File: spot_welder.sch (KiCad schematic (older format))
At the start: 30 parts, among them J1 Conn_01x02_Female, J2 Conn_01x02_Female, J3 Supply, Q1 BSR20, Q2 BSR20, Q3 BSR20, SW1 Rotary_Encoder_Switch, U1 Stm8S103F6_module, U5 MOC3062M

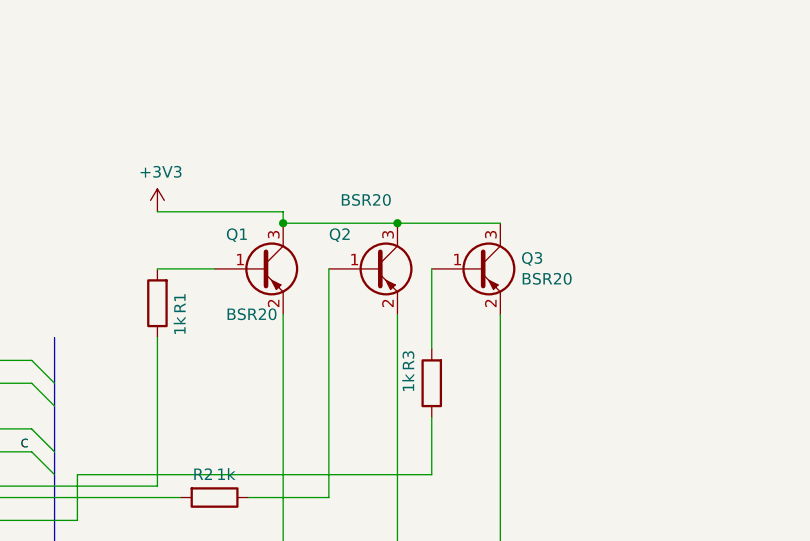
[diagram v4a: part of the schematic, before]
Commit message: clearances increased, vias enlarged
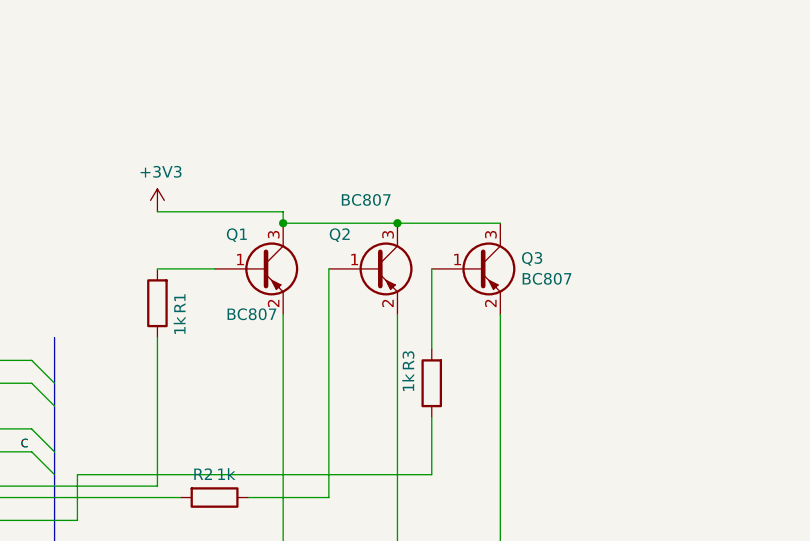
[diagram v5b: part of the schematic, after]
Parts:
- Q1, Q2, Q3: value BSR20 -> BC807
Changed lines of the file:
@@
 P 5000 2550
 F 0 "Q1" H 4850 2700 50  0000 L CNN
-F 1 "BSR20" H 4850 2350 50  0000 L CNN
+F 1 "BC807" H 4850 2350 50  0000 L CNN
 F 2 "Package_TO_SOT_SMD:SOT-23" H 5200 2650 50  0001 C CNN
 F 3 "~" H 5000 2550 50  0001 C CNN
@@
 P 5500 2550
 F 0 "Q2" H 5300 2700 50  0000 L CNN
-F 1 "BSR20" H 5350 2850 50  0000 L CNN
+F 1 "BC807" H 5350 2850 50  0000 L CNN
 F 2 "Package_TO_SOT_SMD:SOT-23" H 5700 2650 50  0001 C CNN
 F 3 "~" H 5500 2550 50  0001 C CNN
@@
 P 5950 2550
 F 0 "Q3" H 6141 2596 50  0000 L CNN
-F 1 "BSR20" H 6141 2505 50  0000 L CNN
+F 1 "BC807" H 6141 2505 50  0000 L CNN
 F 2 "Package_TO_SOT_SMD:SOT-23" H 6150 2650 50  0001 C CNN
 F 3 "~" H 5950 2550 50  0001 C CNN

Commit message: library name updated
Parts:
- D2: symbol marcin_schematic:SM410363 -> marcin_kicad_sch:SM410363
- U1: symbol marcin_schematic:Stm8S103F6_module -> marcin_kicad_sch:Stm8S103F6_module
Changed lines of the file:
@@
 EESchema Schematic File Version 4
-LIBS:spot_welder-cache
-EELAYER 26 0
+EELAYER 30 0
 EELAYER END
 $Descr A4 11693 8268
@@
 	2550 6250 2550 6300
 $Comp
-L marcin_schematic:Stm8S103F6_module U1
+L marcin_kicad_sch:Stm8S103F6_module U1
 U 1 1 5EED1B37
 P 2450 2950
@@
 	2200 2750 2200 2950
 $Comp
-L marcin_schematic:SM410363 D2
+L marcin_kicad_sch:SM410363 D2
 U 1 1 5EF29973
 P 4950 4250
